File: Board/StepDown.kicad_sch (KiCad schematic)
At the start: 19 parts, among them U4 TPS548A20RVER

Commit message: Version 2
- Fixed StepDown stabilization 5V output - probebly idk :D
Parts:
- removed C24, C25: 47uF, Capacitor_SMD:C_0805_2012Metric, symbol Device:C
- added C24, C25: 100uF, Capacitor_SMD:C_Elec_6.3x5.4, symbol Device:C_Polarized
- added C31: 47uF, Capacitor_SMD:C_0805_2012Metric, symbol Device:C
- R36: value 100k -> 1n
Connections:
- net Earth: now also C24.2, C25.2, C31.2
- net Vout: now also C24.1, C25.1, C31.1

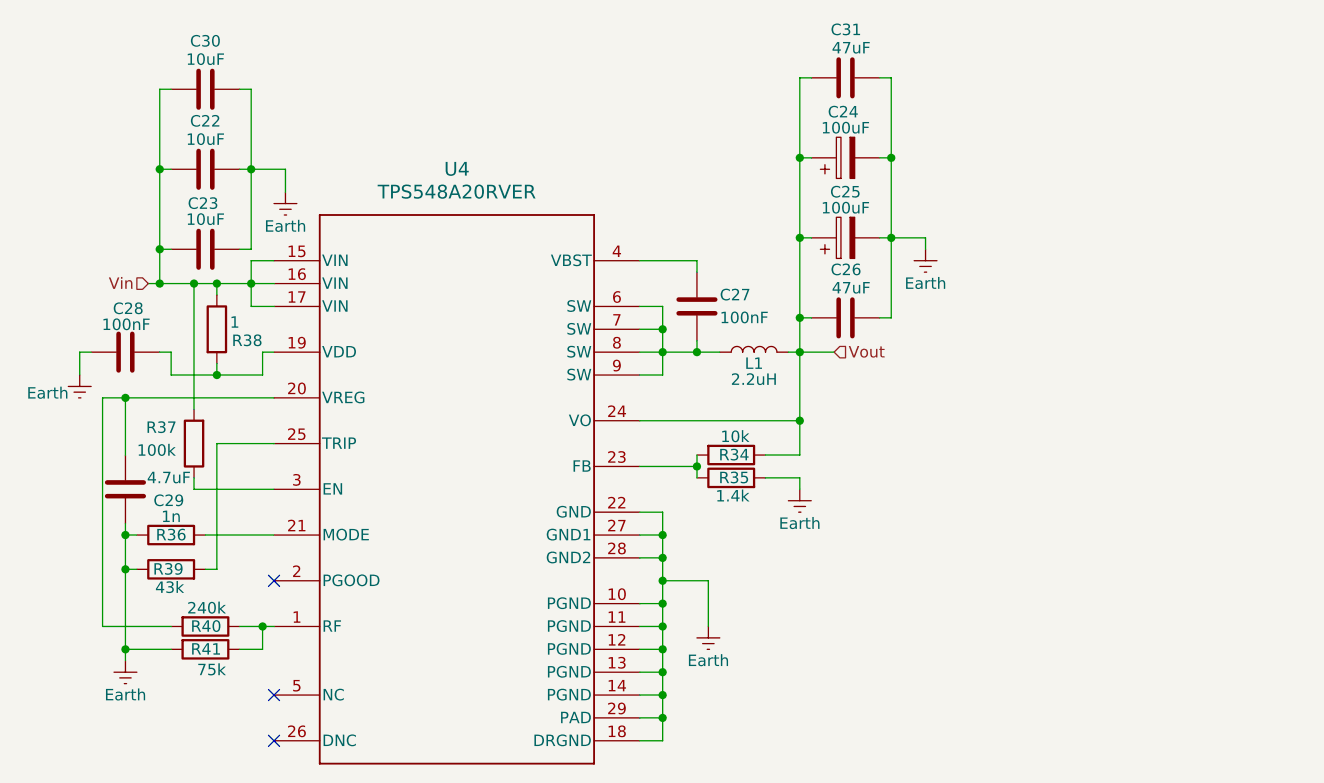
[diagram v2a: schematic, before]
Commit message: Total Power Suply layout overhall
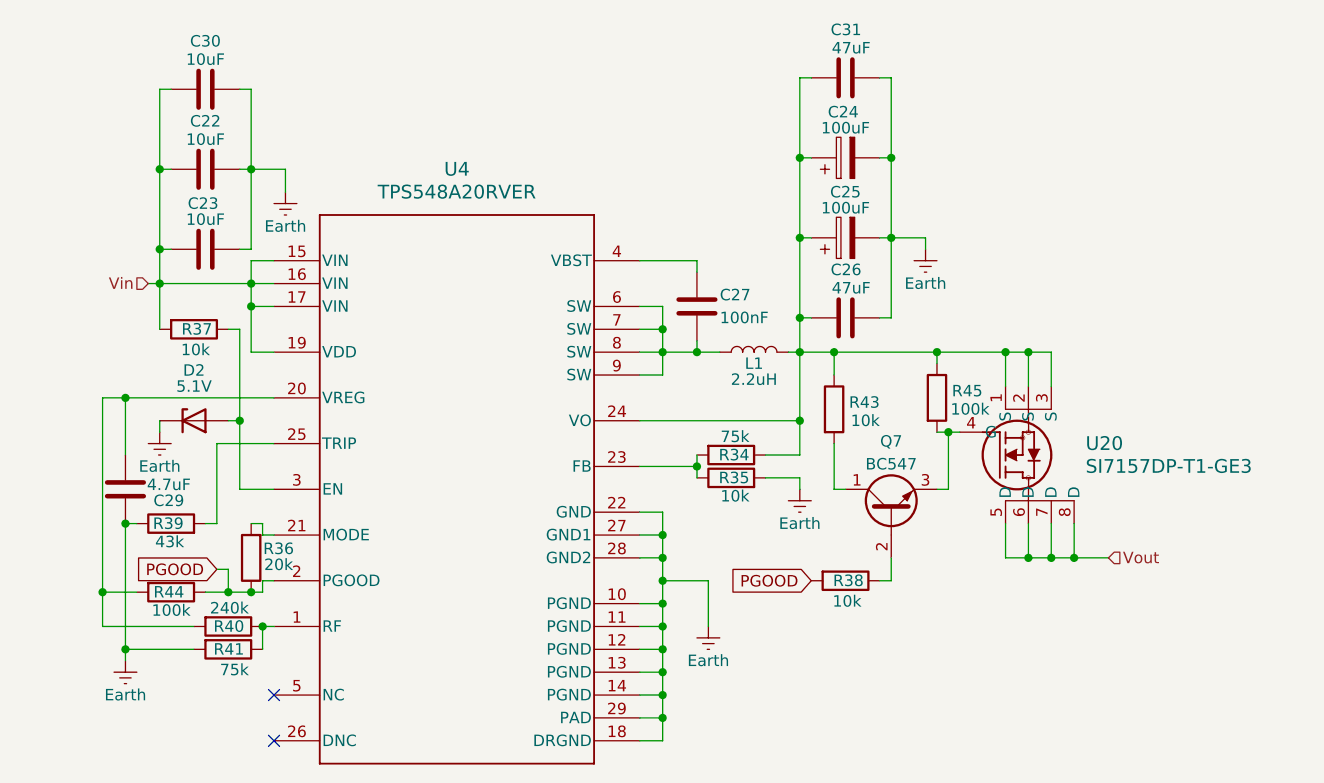
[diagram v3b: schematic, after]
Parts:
- removed C28: 100nF, Capacitor_SMD:C_0805_2012Metric, symbol Device:C
- added D2: 5.1V, Diode_SMD:D_SOD-123, symbol Device:D_Zener
- added Q7: BC547, Package_TO_SOT_SMD:SOT-23, symbol Transistor_BJT:BC547
- added R43: 10k, Resistor_SMD:R_0603_1608Metric, symbol Device:R
- added R44, R45: 100k, Resistor_SMD:R_0603_1608Metric, symbol Device:R
- added U20: SI7157DP-T1-GE3, Package_SO:PowerPAK_SO-8_Dual, symbol Library:SI7157DP-T1-GE3
- R34: value 10k -> 75k
- R35: value 1.4k -> 10k
- R36: value 1n -> 20k
- R37: value 100k -> 10k
- R38: value 1 -> 10k
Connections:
- net Earth: now also D2.1 (K); no longer R36.1
- net Vin: now also U4.19 (VDD); no longer R38.1
- net Vout: now also U20.5 (D), U20.6 (D), U20.7 (D), U20.8 (D); no longer C24.1, C25.1, C26.1, C31.1, L1.2, R34.1, U4.24 (VO)
- net PGOOD: now reaches R38.2
- net PGOOD: now also R36.1, U4.2 (PGOOD), R44.1; no longer U4.19 (VDD)
- net at C29.2, R40.2, U4.20 (VREG): now also R44.2
- net at R37.1, U4.3 (EN): now also D2.2 (A)
- new net: C24.1, C25.1, C26.1, C31.1, L1.2, R34.1, R43.1, R45.1, U20.1 (S), U20.2 (S), U20.3 (S), U4.24 (VO)
- new net: Q7.2 (B), R38.1
- new net: Q7.3 (E), R45.2, U20.4 (G)
- new net: Q7.1 (C), R43.2
- no-connect marks 3 -> 2
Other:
- moved on the sheet: R36, R39, R40, R41

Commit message: New Power
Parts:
- removed Q7: BC547, Package_TO_SOT_SMD:SOT-23, symbol Transistor_BJT:BC547
- removed R38, R43: 10k, Resistor_SMD:R_0603_1608Metric, symbol Device:R
- removed R44, R45: 100k, Resistor_SMD:R_0603_1608Metric, symbol Device:R
- removed U20: SI7157DP-T1-GE3, Package_SO:PowerPAK_SO-8_Dual, symbol Library:SI7157DP-T1-GE3
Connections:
- net Vout: now also C24.1, C25.1, C26.1, C31.1, L1.2, R34.1, U4.24 (VO)
- net PGOOD: no longer names the net of R36.1, U4.2 (PGOOD)
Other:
- moved on the sheet: R36

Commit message: Fixed zener diode orientation
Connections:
- net Earth: now also D2.2 (A); no longer D2.1 (K)
- net at R37.1, U4.3 (EN): now also D2.1 (K); no longer D2.2 (A)
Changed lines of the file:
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@@
-	)
-	(symbol
-		(lib_id "Device:D_Zener")
-		(at 74.93 72.39 0)
-		(unit 1)
-		(body_style 1)
-		(exclude_from_sim no)
-		(in_bom yes)
-		(on_board yes)
-		(in_pos_files yes)
-		(dnp no)
-		(property "Reference" "D2"
-			(at 74.93 66.802 0)
-			(show_name no)
-			(do_not_autoplace no)
-			(effects
-				(font
-					(size 1.27 1.27)
-				)
-			)
-		)
-		(property "Value" "5.1V"
-			(at 74.93 68.58 0)
-			(show_name no)
-			(do_not_autoplace no)
-			(effects
-				(font
-					(size 1.27 1.27)
-				)
-			)
-		)
-		(property "Footprint" "Diode_SMD:D_SOD-123"
-			(at 74.93 72.39 0)
-			(hide yes)
-			(show_name no)
-			(do_not_autoplace no)
-			(effects
-				(font
-					(size 1.27 1.27)
-				)
-			)
-		)
-		(property "Datasheet" ""
-			(at 74.93 72.39 0)
-			(hide yes)
-			(show_name no)
-			(do_not_autoplace no)
-			(effects
-				(font
-					(size 1.27 1.27)
-				)
-			)
-		)
-		(property "Description" "Zener diode"
-			(at 74.93 72.39 0)
-			(hide yes)
-			(show_name no)
-			(do_not_autoplace no)
-			(effects
-				(font
-					(size 1.27 1.27)
-				)
-			)
-		)
-		(pin "1"
-		)
-		(pin "2"
-		)
-		(instances
-			(project "SlimeVR_Dock"
-				(path "/06ff9557-1f9b-4670-8a34-bb7684a016dd/9328ec89-1532-462d-95ef-1baa495e4b70"
-					(reference "D2")
-					(unit 1)
-				)
-			)
-		)
 	)
 	(symbol
@@
 					(unit 1)
 				)
+			)
+		)
+	)
+	(symbol
+		(lib_id "Device:D_Zener")
+		(at 74.93 72.39 180)
+		(unit 1)
+		(body_style 1)
+		(exclude_from_sim no)
+		(in_bom yes)
+		(on_board yes)
+		(in_pos_files yes)
+		(dnp no)
+		(property "Reference" "D2"
+			(at 74.93 68.58 0)
+			(show_name no)
+			(do_not_autoplace no)
+			(effects
+				(font
+					(size 1.27 1.27)
+				)
+			)
+		)
+		(property "Value" "5.1V"
+			(at 74.93 66.802 0)
+			(show_name no)
+			(do_not_autoplace no)
+			(effects
+				(font
+					(size 1.27 1.27)
+				)
+			)
+		)
+		(property "Footprint" "Diode_SMD:D_SOD-123"
+			(at 74.93 72.39 0)
+			(hide yes)
+			(show_name no)
+			(do_not_autoplace no)
+			(effects
+				(font
+					(size 1.27 1.27)
+				)
+			)
+		)
+		(property "Datasheet" ""
+			(at 74.93 72.39 0)
+			(hide yes)
+			(show_name no)
+			(do_not_autoplace no)
+			(effects
+				(font
+					(size 1.27 1.27)
+				)
+			)
+		)
+		(property "Description" "Zener diode"
+			(at 74.93 72.39 0)
+			(hide yes)
+			(show_name no)
+			(do_not_autoplace no)
+			(effects
+				(font
+					(size 1.27 1.27)
+				)
+			)
+		)
+		(pin "1"
+		)
+		(pin "2"
+		)
+		(instances
+			(project "SlimeVR_Dock"
+				(path "/06ff9557-1f9b-4670-8a34-bb7684a016dd/9328ec89-1532-462d-95ef-1baa495e4b70"
+					(reference "D2")
+					(unit 1)
+				)

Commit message: Version 3
Hopefully it works idk ?:D
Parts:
- R37: value 10k -> 4k7
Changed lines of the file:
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@@
 			)
 		)
-		(property "Value" "10k"
+		(property "Value" "4k7"
 			(at 76.708 64.516 90)
 			(show_name no)

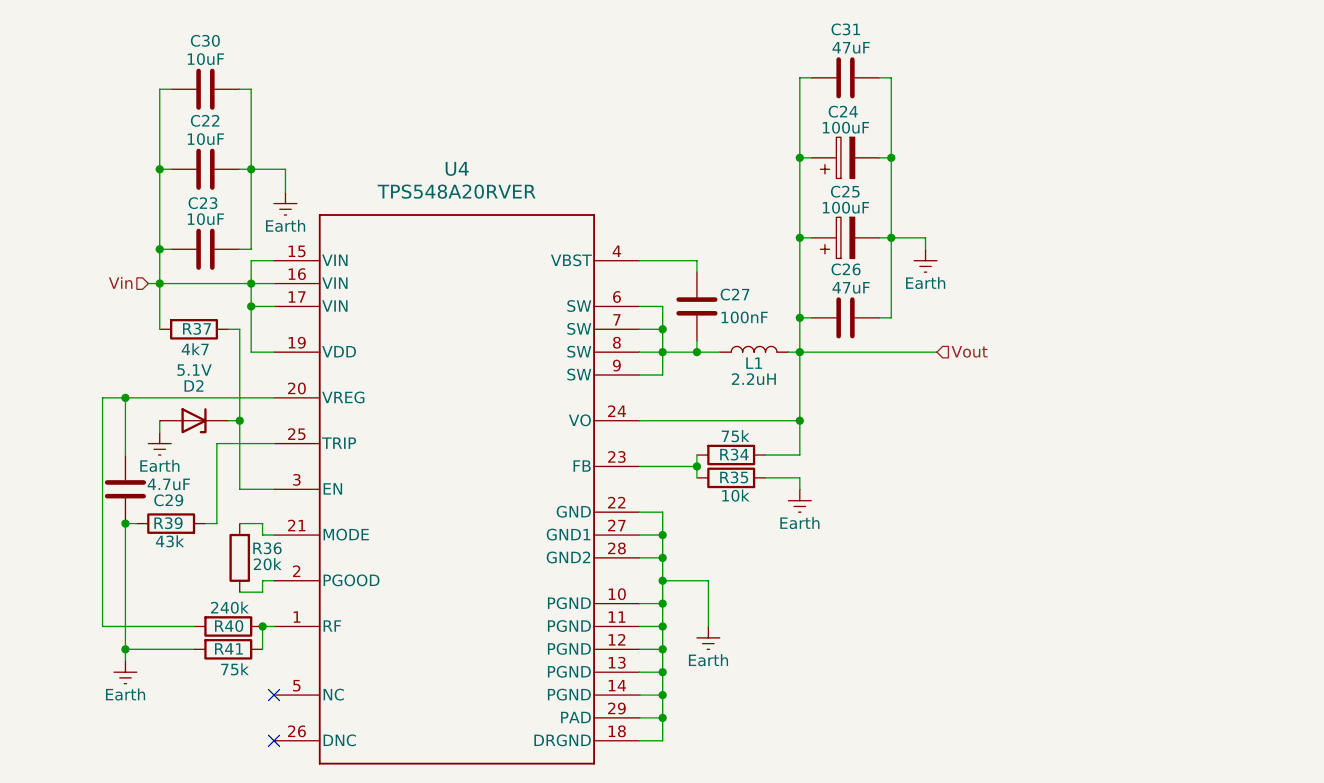
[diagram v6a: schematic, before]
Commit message: RC on coil outut and VDD resistor added
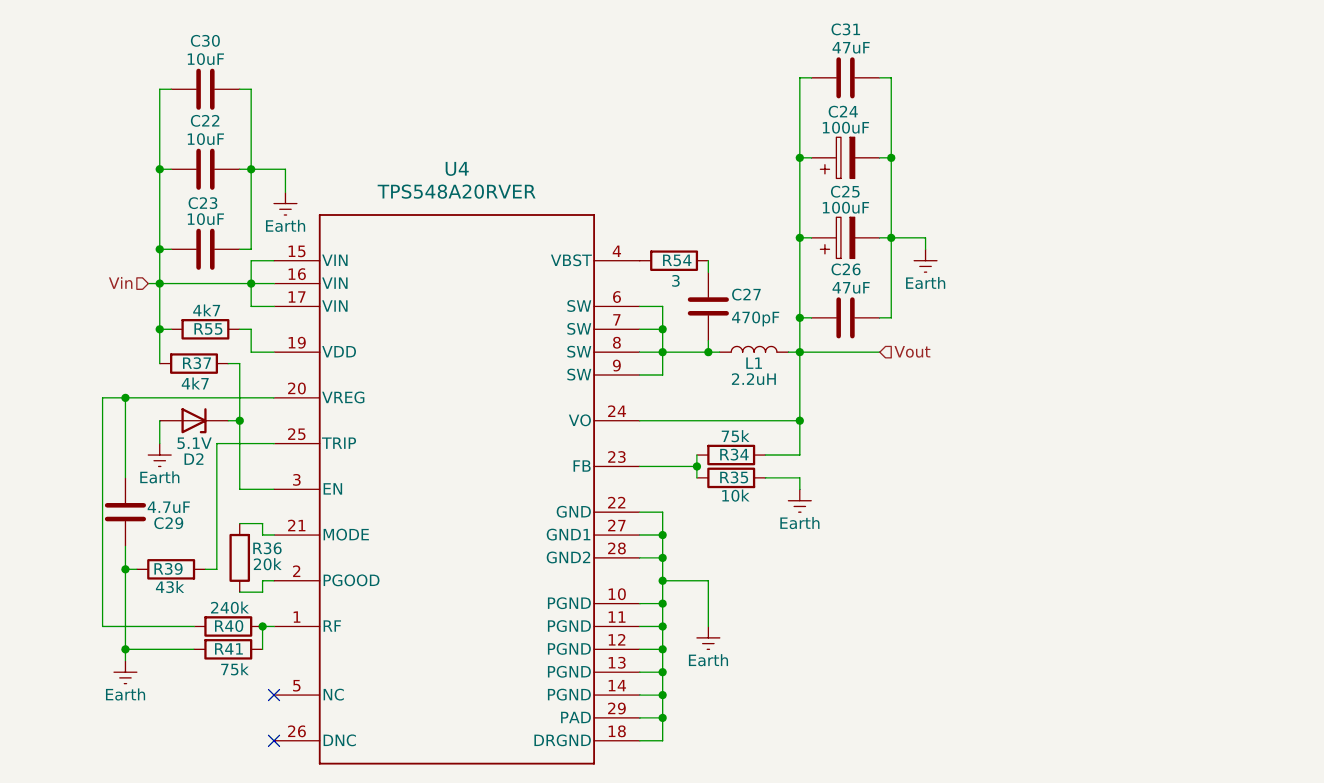
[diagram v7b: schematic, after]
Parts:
- added R54: 3, Resistor_SMD:R_0805_2012Metric, symbol Device:R
- added R55: 4k7, Resistor_SMD:R_0603_1608Metric, symbol Device:R
- C27: value 100nF -> 470pF
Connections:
- net Vin: now also R55.2; no longer U4.19 (VDD)
- net at C27.1: now also R54.1; no longer U4.4 (VBST)
- new net: R55.1, U4.19 (VDD)
- new net: R54.2, U4.4 (VBST)
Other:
- moved on the sheet: C27, C29, R37, R39

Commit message: Changed baed on sugestions
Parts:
- removed D2: 5.1V, Diode_SMD:D_SOD-123, symbol Device:D_Zener
- added R56: 100k, Resistor_SMD:R_0603_1608Metric, symbol Device:R
- added R57: 10k, Resistor_SMD:R_0603_1608Metric, symbol Device:R
- R37: value 4k7 -> 75k
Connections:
- net Earth: now also R56.1, R57.2
- net at R37.1, U4.3 (EN): now also R57.1
- net at R36.1, U4.2 (PGOOD): now also R56.2
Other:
- moved on the sheet: R39
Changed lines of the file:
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@@
+	)
+	(junction
+		(at 67.31 91.44)
+		(diameter 0)
+		(color 0 0 0 0)
 	)
 	(junction
@@
 	)
 	(junction
+		(at 67.31 86.36)
+		(diameter 0)
+		(color 0 0 0 0)
+	)
+	(junction
 		(at 127 64.77)
+		(diameter 0)
+		(color 0 0 0 0)
+	)
+	(junction
+		(at 80.01 91.44)
 		(diameter 0)
 		(color 0 0 0 0)
@@
 	)
 	(junction
-		(at 67.31 88.9)
-		(diameter 0)
-		(color 0 0 0 0)
-	)
-	(junction
 		(at 71.12 44.45)
 		(diameter 0)
@@
 	(wire
 		(pts
+			(xy 76.2 91.44) (xy 80.01 91.44)
+		)
+		(stroke
+			(width 0)
+			(type default)
+		)
+	)
+	(wire
+		(pts
 			(xy 80.01 91.44) (xy 82.55 91.44)
 		)
@@
 	(wire
 		(pts
-			(xy 67.31 88.9) (xy 67.31 86.36)
-		)
-		(stroke
-			(width 0)
-			(type default)
-		)
-	)
-	(wire
-		(pts
 			(xy 67.31 69.85) (xy 67.31 78.74)
 		)
@@
 	(wire
 		(pts
-			(xy 77.47 88.9) (xy 76.2 88.9)
+			(xy 77.47 86.36) (xy 76.2 86.36)
 		)
 		(stroke
@@
 	(wire
 		(pts
-			(xy 67.31 88.9) (xy 68.58 88.9)
+			(xy 67.31 86.36) (xy 68.58 86.36)
 		)
 		(stroke
@@
 	(wire
 		(pts
+			(xy 67.31 91.44) (xy 68.58 91.44)
+		)
+		(stroke
+			(width 0)
+			(type default)
+		)
+	)
+	(wire
+		(pts
 			(xy 127 59.69) (xy 127 62.23)
 		)
@@
 	(wire
 		(pts
-			(xy 77.47 74.93) (xy 77.47 88.9)
+			(xy 77.47 74.93) (xy 77.47 86.36)
 		)
 		(stroke
@@
 	(wire
 		(pts
-			(xy 67.31 88.9) (xy 67.31 97.79)
-		)
-		(stroke
-			(width 0)
-			(type default)
-		)
-	)
-	(wire
-		(pts
 			(xy 64.77 69.85) (xy 67.31 69.85)
 		)
@@
 	(wire
 		(pts
+			(xy 67.31 86.36) (xy 67.31 91.44)
+		)
+		(stroke
+			(width 0)
+			(type default)
+		)
+	)
+	(wire
+		(pts
 			(xy 124.46 64.77) (xy 127 64.77)
 		)
@@
 		(pts
 			(xy 132.08 54.61) (xy 132.08 55.88)
+		)
+		(stroke
+			(width 0)
+			(type default)
+		)
+	)
+	(wire
+		(pts
+			(xy 67.31 91.44) (xy 67.31 97.79)
 		)
 		(stroke
@@
 	)
 	(symbol
+		(lib_id "Device:R")
+		(at 74.93 72.39 270)
+		(unit 1)
+		(body_style 1)
+		(exclude_from_sim no)
+		(in_bom yes)
+		(on_board yes)
+		(in_pos_files yes)
+		(dnp no)
+		(property "Reference" "R57"
+			(at 76.962 72.39 90)
+			(show_name no)
+			(do_not_autoplace no)
+			(effects
+				(font
+					(size 1.27 1.27)
+				)
+				(justify right)
+			)
+		)
+		(property "Value" "10k"
+			(at 76.708 74.93 90)
+			(show_name no)
+			(do_not_autoplace no)
+			(effects
+				(font
+					(size 1.27 1.27)
+				)
+				(justify right)
+			)
+		)
+		(property "Footprint" "Resistor_SMD:R_0603_1608Metric"
+			(at 74.93 70.612 90)
+			(hide yes)
+			(show_name no)
+			(do_not_autoplace no)
+			(effects
+				(font
+					(size 1.27 1.27)
+				)
+			)
+		)
+		(property "Datasheet" ""
+			(at 74.93 72.39 0)
+			(hide yes)
+			(show_name no)
+			(do_not_autoplace no)
+			(effects
+				(font
+					(size 1.27 1.27)
+				)
+			)
+		)
+		(property "Description" "Resistor"
+			(at 74.93 72.39 0)
+			(hide yes)
+			(show_name no)
+			(do_not_autoplace no)
+			(effects
+				(font
+					(size 1.27 1.27)
+				)
+			)
+		)
+		(pin "1"
+		)
+		(pin "2"
+		)
+		(instances
+			(project "SlimeVR_Dock"
+				(path "/06ff9557-1f9b-4670-8a34-bb7684a016dd/9328ec89-1532-462d-95ef-1baa495e4b70"
+					(reference "R57")
+					(unit 1)
+				)
+			)
+		)
+	)
+	(symbol
 		(lib_id "power:Earth")
 		(at 67.31 99.06 0)
@@
 				(path "/06ff9557-1f9b-4670-8a34-bb7684a016dd/9328ec89-1532-462d-95ef-1baa495e4b70"
 					(reference "#PWR090")
-					(unit 1)
-				)
-			)
-		)
-	)
-	(symbol
-		(lib_id "Device:D_Zener")
-		(at 74.93 72.39 180)
-		(unit 1)
-		(body_style 1)
-		(exclude_from_sim no)
-		(in_bom yes)
-		(on_board yes)
-		(in_pos_files yes)
-		(dnp no)
-		(property "Reference" "D2"
-			(at 74.93 76.708 0)
-			(show_name no)
-			(do_not_autoplace no)
-			(effects
-				(font
-					(size 1.27 1.27)
-				)
-			)
-		)
-		(property "Value" "5.1V"
-			(at 74.93 74.93 0)
-			(show_name no)
-			(do_not_autoplace no)
-			(effects
-				(font
-					(size 1.27 1.27)
-				)
-			)
-		)
-		(property "Footprint" "Diode_SMD:D_SOD-123"
-			(at 74.93 72.39 0)
-			(hide yes)
-			(show_name no)
-			(do_not_autoplace no)
-			(effects
-				(font
-					(size 1.27 1.27)
-				)
-			)
-		)
-		(property "Datasheet" ""
-			(at 74.93 72.39 0)
-			(hide yes)
-			(show_name no)
-			(do_not_autoplace no)
-			(effects
-				(font
-					(size 1.27 1.27)
-				)
-			)
-		)
-		(property "Description" "Zener diode"
-			(at 74.93 72.39 0)
-			(hide yes)
-			(show_name no)
-			(do_not_autoplace no)
-			(effects
-				(font
-					(size 1.27 1.27)
-				)
-			)
-		)
-		(pin "1"
-		)
-		(pin "2"
-		)
-		(instances
-			(project "SlimeVR_Dock"
-				(path "/06ff9557-1f9b-4670-8a34-bb7684a016dd/9328ec89-1532-462d-95ef-1baa495e4b70"
-					(reference "D2")
 					(unit 1)
 				)
@@
 			)
 		)
-		(property "Value" "4k7"
+		(property "Value" "75k"
 			(at 76.708 68.326 90)
 			(show_name no)
@@
 	(symbol
 		(lib_id "Device:R")
-		(at 72.39 88.9 90)
+		(at 72.39 86.36 90)
 		(unit 1)
 		(body_style 1)
@@
 		(dnp no)
 		(property "Reference" "R39"
-			(at 70.358 88.9 90)
+			(at 70.358 86.36 90)
 			(show_name no)
 			(do_not_autoplace no)
@@
 		)
 		(property "Value" "43k"
-			(at 70.612 90.932 90)
+			(at 70.612 88.392 90)
 			(show_name no)
 			(do_not_autoplace no)
@@
 		)
 		(property "Footprint" "Resistor_SMD:R_0603_1608Metric"
-			(at 72.39 90.678 90)
+			(at 72.39 88.138 90)
 			(hide yes)
 			(show_name no)
@@
 		)
 		(property "Datasheet" ""
-			(at 72.39 88.9 0)
+			(at 72.39 86.36 0)
 			(hide yes)
 			(show_name no)
@@
 		)
 		(property "Description" "Resistor"
-			(at 72.39 88.9 0)
+			(at 72.39 86.36 0)
 			(hide yes)
 			(show_name no)
@@
 					(unit 1)
 				)
+			)
+		)
+	)
+	(symbol
+		(lib_id "Device:R")
+		(at 72.39 91.44 90)
+		(unit 1)
+		(body_style 1)
+		(exclude_from_sim no)
+		(in_bom yes)
+		(on_board yes)
+		(in_pos_files yes)
+		(dnp no)
+		(property "Reference" "R56"
+			(at 70.358 91.44 90)
+			(show_name no)
+			(do_not_autoplace no)
+			(effects
+				(font
+					(size 1.27 1.27)
+				)
+				(justify right)
+			)
+		)
+		(property "Value" "100k"
+			(at 70.104 93.472 90)
+			(show_name no)
+			(do_not_autoplace no)
+			(effects
+				(font
+					(size 1.27 1.27)
+				)
+				(justify right)
+			)
+		)
+		(property "Footprint" "Resistor_SMD:R_0603_1608Metric"
+			(at 72.39 93.218 90)
+			(hide yes)
+			(show_name no)
+			(do_not_autoplace no)
+			(effects
+				(font
+					(size 1.27 1.27)
+				)
+			)
+		)
+		(property "Datasheet" ""
+			(at 72.39 91.44 0)
+			(hide yes)
+			(show_name no)
+			(do_not_autoplace no)
+			(effects
+				(font
+					(size 1.27 1.27)
+				)
+			)
+		)
+		(property "Description" "Resistor"
+			(at 72.39 91.44 0)
+			(hide yes)
+			(show_name no)
+			(do_not_autoplace no)
+			(effects
+				(font
+					(size 1.27 1.27)
+				)
+			)
+		)
+		(pin "1"
+		)
+		(pin "2"
+		)
+		(instances
+			(project "SlimeVR_Dock"
+				(path "/06ff9557-1f9b-4670-8a34-bb7684a016dd/9328ec89-1532-462d-95ef-1baa495e4b70"
+					(reference "R56")
+					(unit 1)
+				)
